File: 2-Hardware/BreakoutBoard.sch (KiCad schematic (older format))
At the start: 1 part

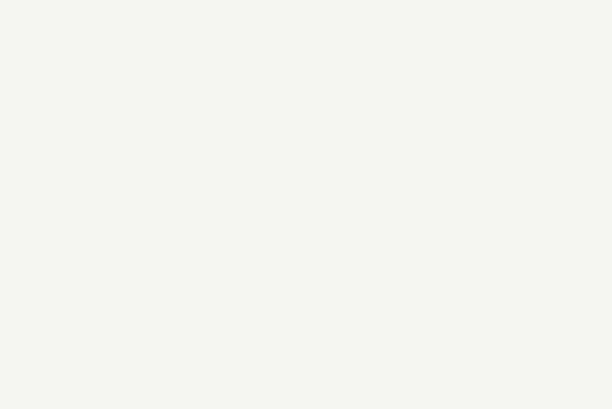
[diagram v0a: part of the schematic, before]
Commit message: Added bus pirate connectors
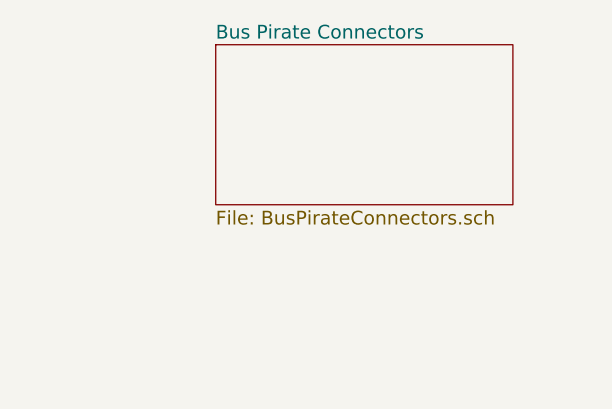
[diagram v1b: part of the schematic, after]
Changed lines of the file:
@@
 LIBS:TransistorParts
 LIBS:CubeSat
-EELAYER 27 0
+LIBS:BreakoutBoard-cache
+EELAYER 25 0
 EELAYER END
 $Descr A4 11693 8268
 encoding utf-8
-Sheet 1 2
+Sheet 1 3
 Title ""
 Date "7 oct 2014"
@@
 F1 "CubeSatBus.sch" 50
 $EndSheet
+$Sheet
+S 7700 4000 1300 700
+U 543726AE
+F0 "Bus Pirate Connectors" 60
+F1 "BusPirateConnectors.sch" 60
+$EndSheet
 $EndSCHEMATC
